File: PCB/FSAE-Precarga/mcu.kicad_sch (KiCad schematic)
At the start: 22 parts, among them J3 Programming Port, SW1 SW_MEC_5E, U6 STM32F103C8Tx, Y1 Crystal

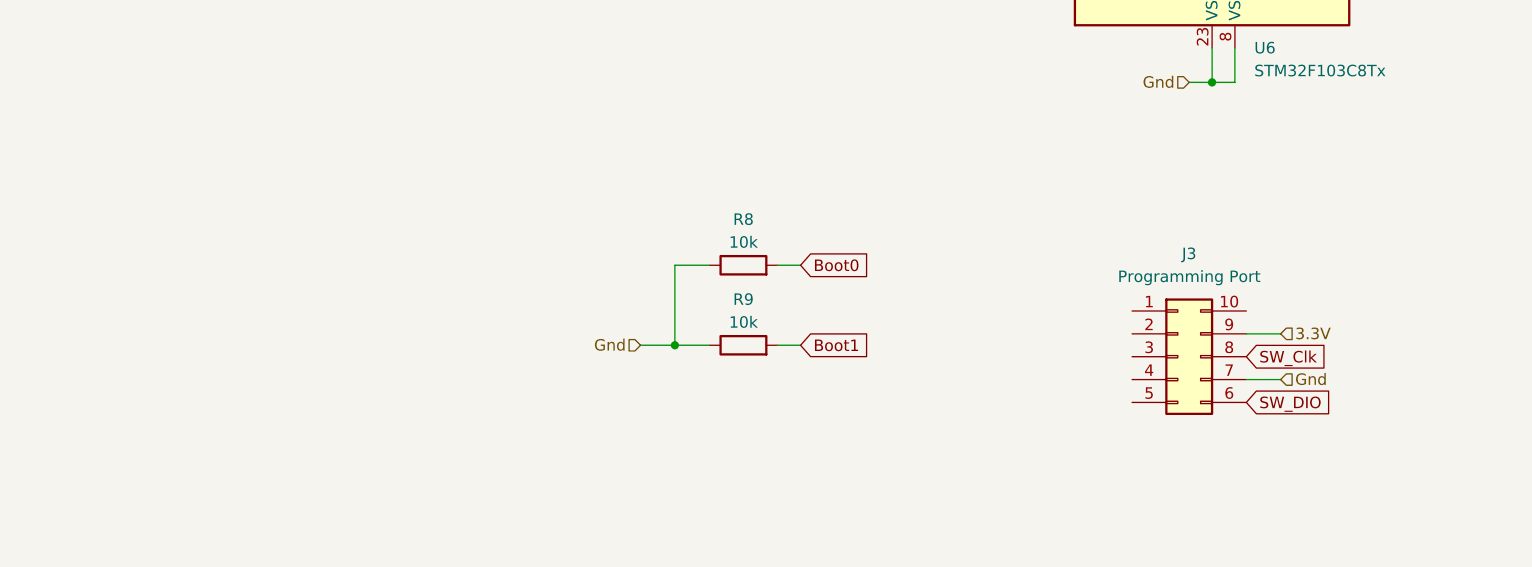
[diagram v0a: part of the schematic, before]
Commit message: Version avanzada de la placa de Precarga
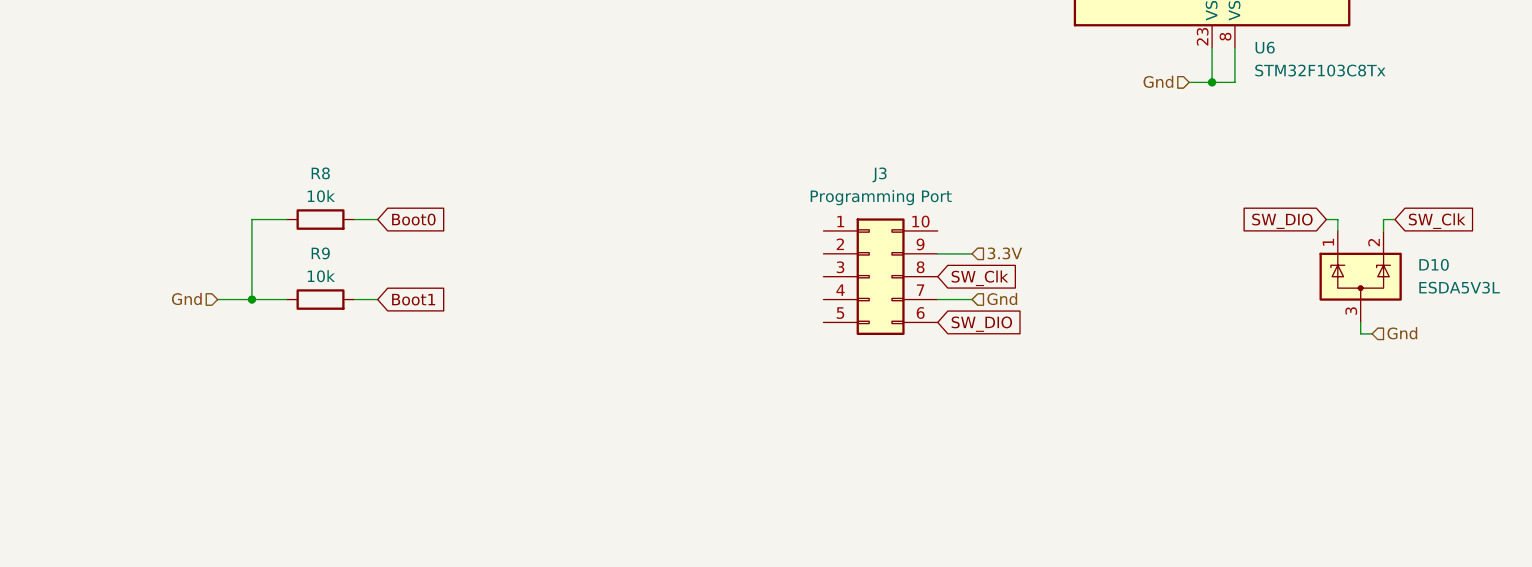
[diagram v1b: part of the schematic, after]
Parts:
- added D10: ESDA5V3L, Package_TO_SOT_SMD:SOT-23-3, symbol Power_Protection:ESDA5V3L
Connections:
- net Gnd: now also D10.3 (A)
- net SW_Clk: now also D10.2 (K)
- net SW_DIO: now also D10.1 (K)
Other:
- moved on the sheet: J3, R8, R9

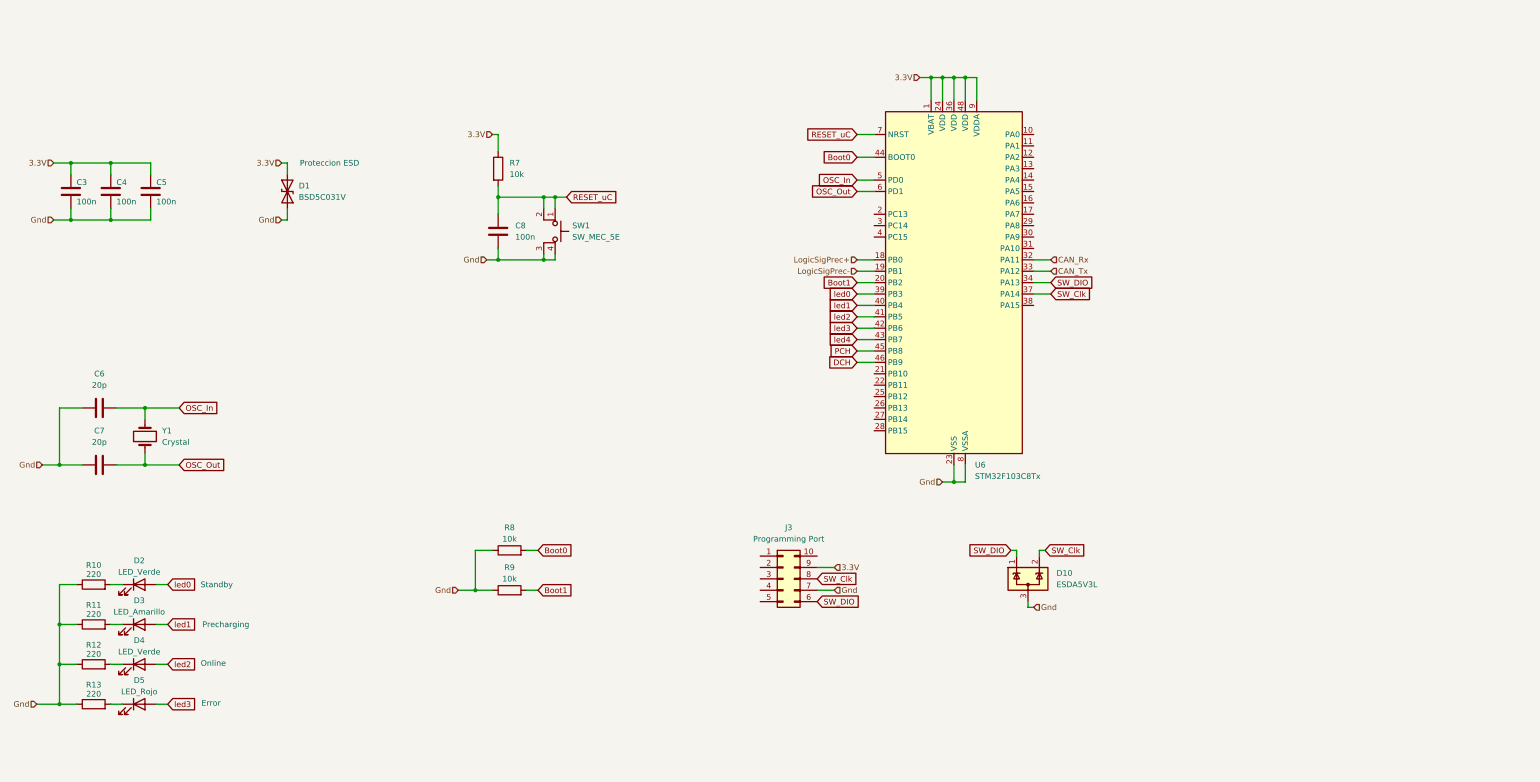
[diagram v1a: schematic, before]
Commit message: Subo correcciones placa de precarga
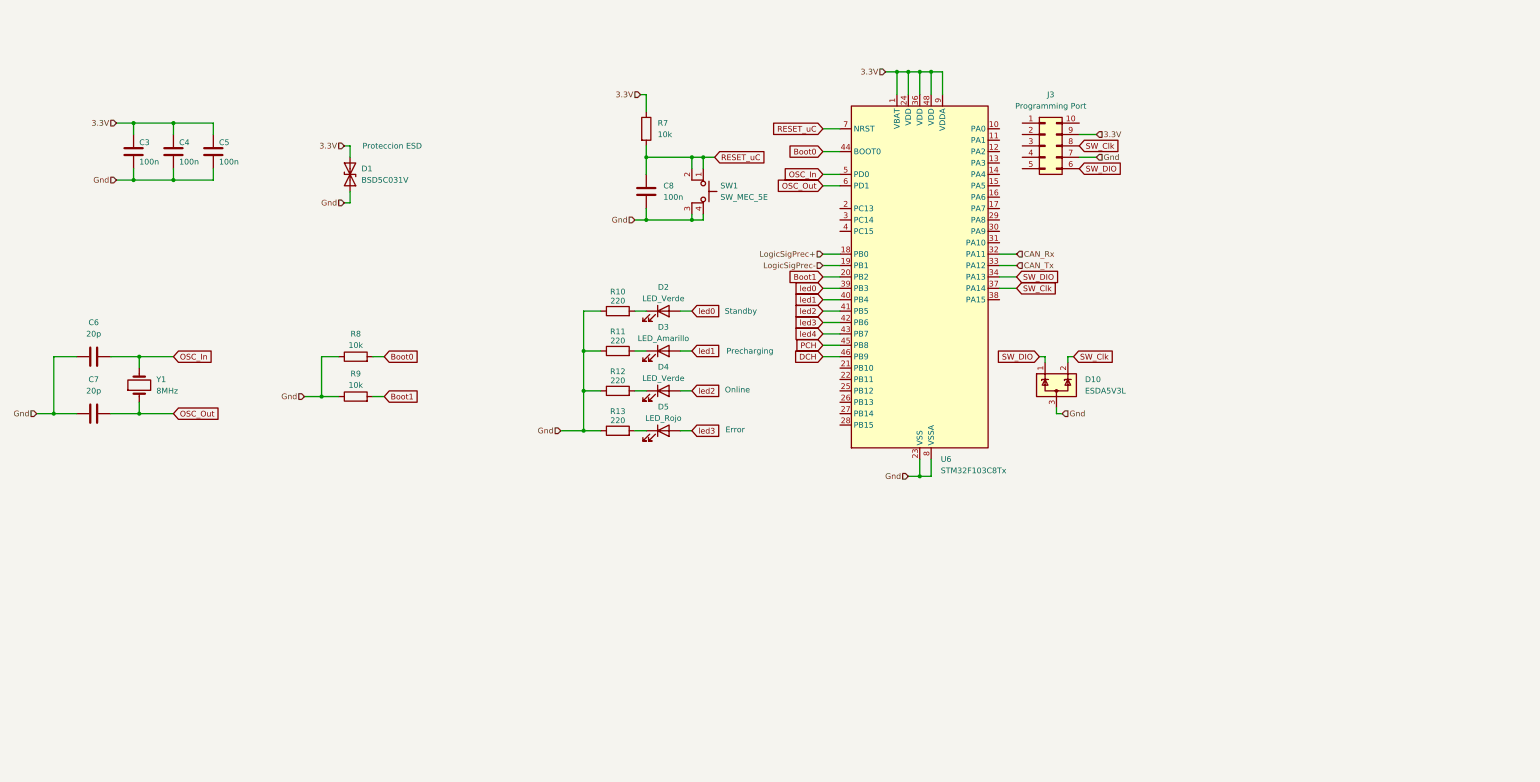
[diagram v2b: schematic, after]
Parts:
- Y1: value Crystal -> 8MHz
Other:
- moved on the sheet: C3, C4, C5, C6, C7, C8, D1, D10, D2, D3, D4, D5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

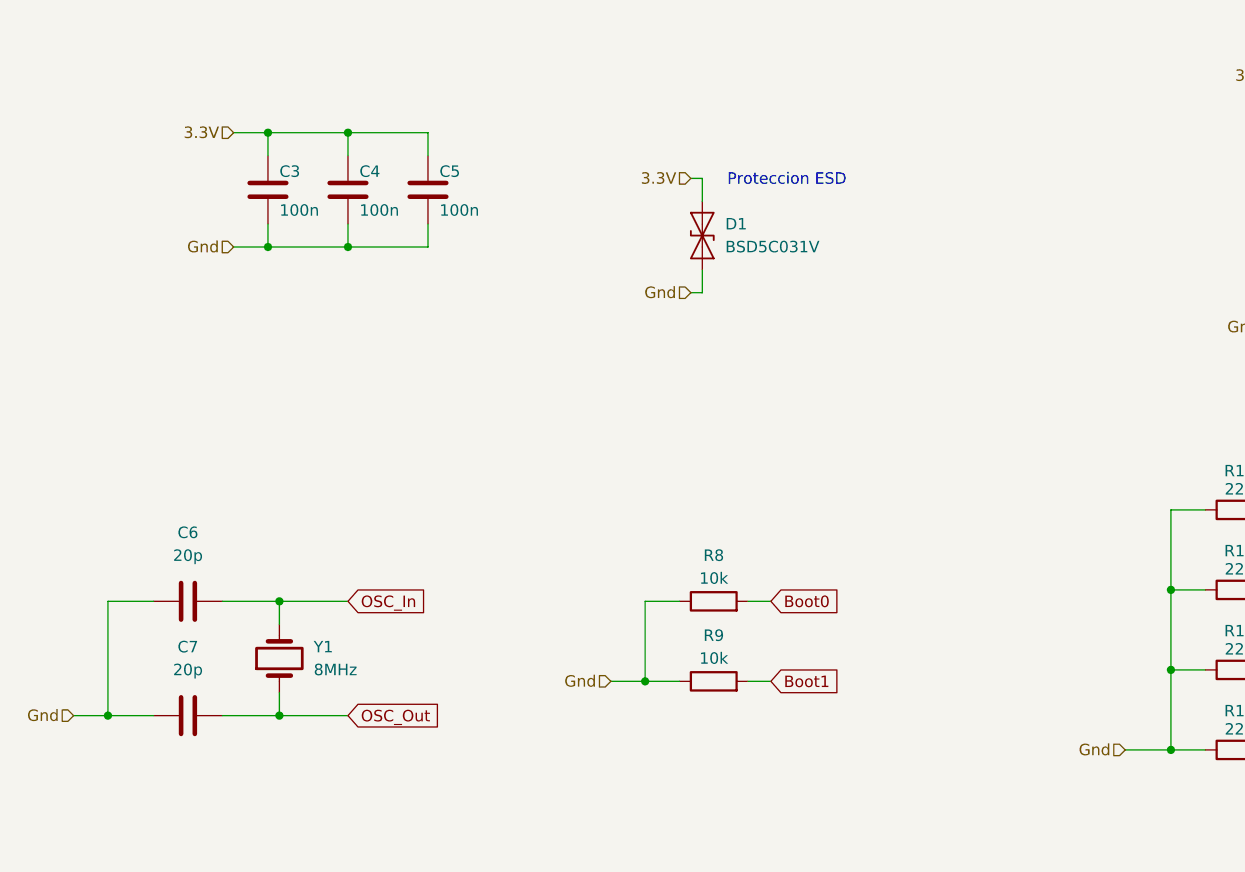
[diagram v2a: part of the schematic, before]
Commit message: Agrego correcciones/agregados placa precarga
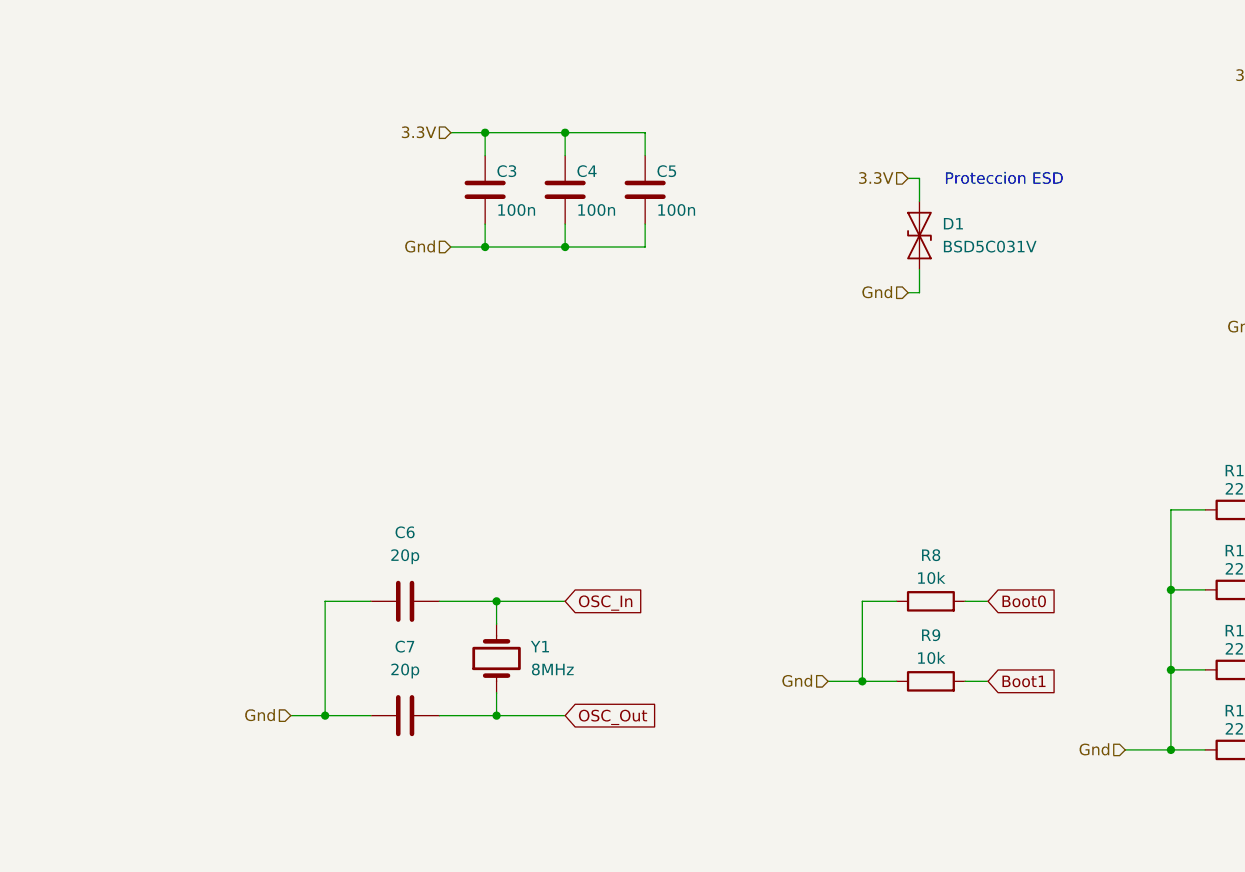
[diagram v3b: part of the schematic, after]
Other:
- moved on the sheet: C3, C4, C5, C6, C7, D1, R8, R9, Y1

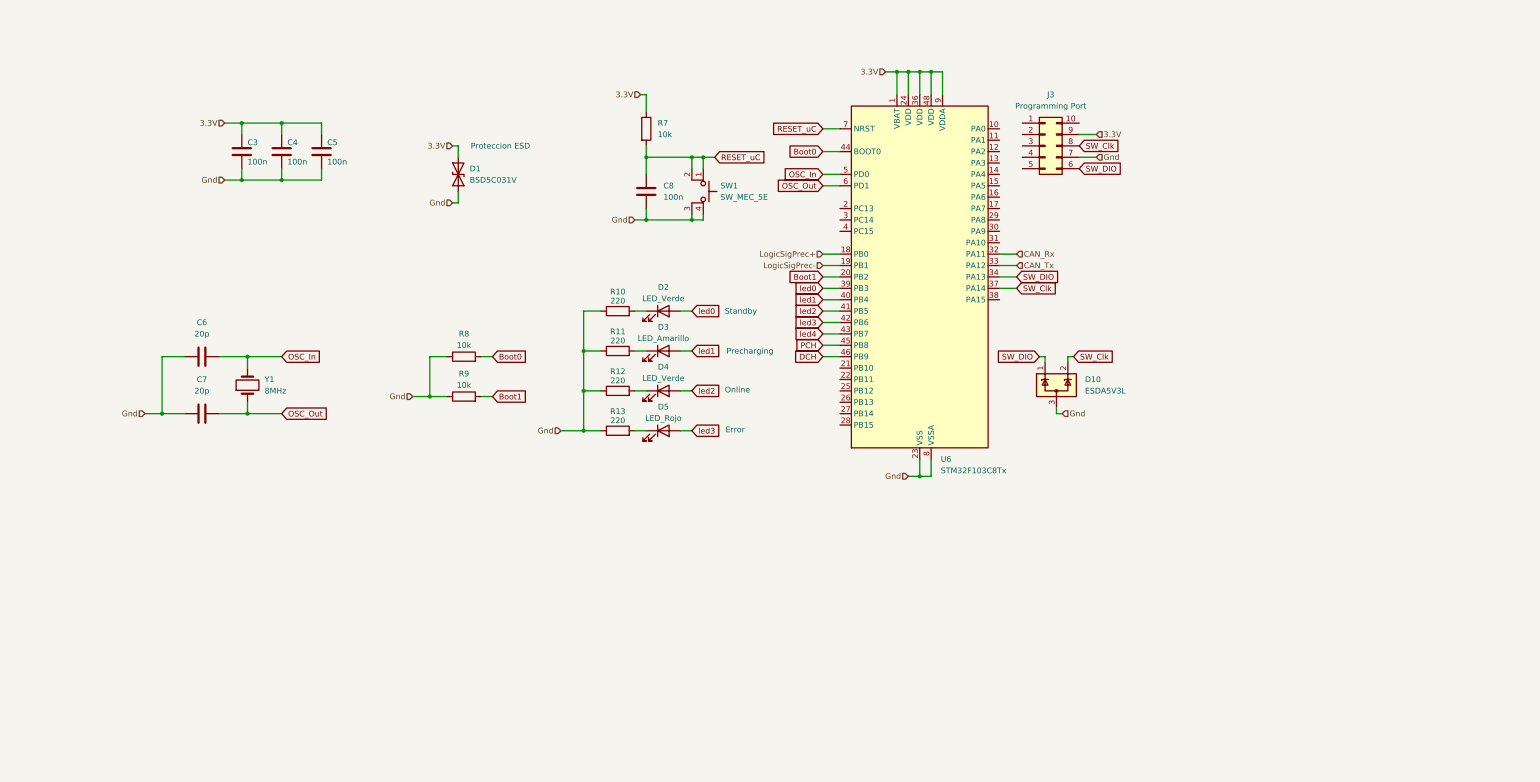
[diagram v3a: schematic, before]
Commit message: Agrego circuito de control/verificacion de los AIR en placa de precarga
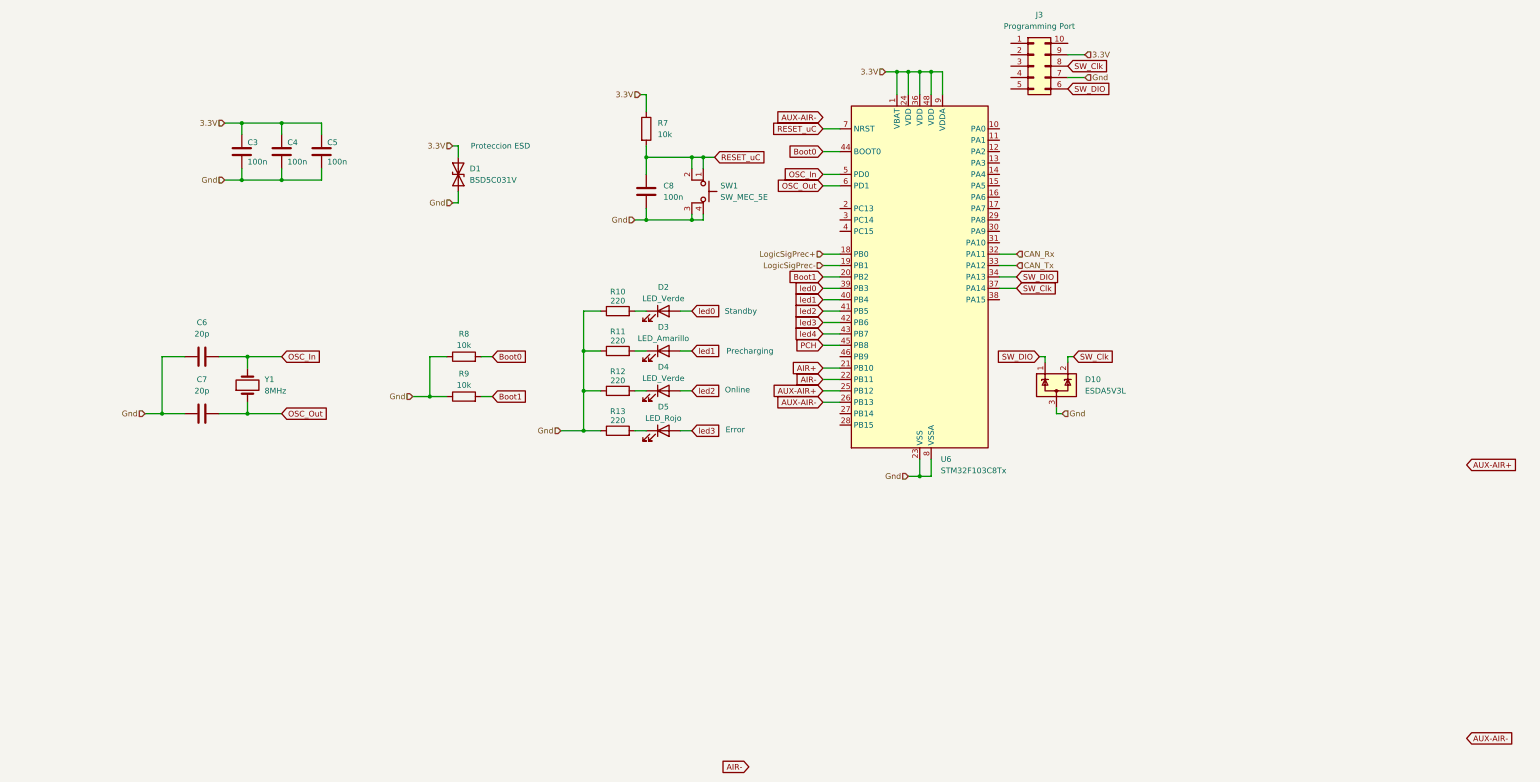
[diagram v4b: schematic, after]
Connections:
- net AIR+: now reaches U6.21 (PB10)
- net AIR-: now reaches U6.22 (PB11)
- net AUX-AIR+: now reaches U6.25 (PB12)
- net AUX-AIR-: now reaches U6.26 (PB13)
- net DCH: no longer names the net of U6.46 (PB9)
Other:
- moved on the sheet: J3
